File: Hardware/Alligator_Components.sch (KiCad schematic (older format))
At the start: 66 parts, among them J1 SWD_Header, J8 Eurorack_16_pin_power, U1 STM32F446RETx, U3 MCP6004, U4 PCM5100APW, U5 TL072, U7 LM1117-3.3, Y1 8MHz 20pF

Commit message: Updates to schematic; Output ADC data over I2S via interrupt with L/R awareness
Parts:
- removed C? (x2): 2.2uF, symbol Device:C_Small
- removed C? (x2): 30pF, symbol Device:C_Small
- removed C? (x6): 100nF, symbol Device:C_Small
- removed J8: Eurorack_16_pin_power, Custom_Footprints:Eurorack_16_pin_header, symbol Eurorack_Header:Eurorack_16_pin_power
- removed U1: STM32F446RETx, Package_QFP:LQFP-64_10x10mm_P0.5mm, symbol MCU_ST_STM32F4:STM32F446RETx
- removed U?: STM32H743VITx, Package_QFP:LQFP-100_14x14mm_P0.5mm, symbol MCU_ST_STM32H7:STM32H743VITx
- added C1, C10, C11, C12, C14, C15, C16, C19, C20, C21, C25, C26, C37, C42, C44, C5, C7, C8, C9: 100nF, symbol Device:C_Small
- added C2, C3: 30pF, symbol Device:C_Small
- added C4, C6: 2.2uF, symbol Device:C_Small
- added J2: Eurorack_10_pin_power, Custom_Footprints:Eurorack_10_pin_header, symbol Eurorack_Header:Eurorack_10_pin_power
- added J3: Conn_01x20_Female, symbol Connector:Conn_01x20_Female
- added U1: STM32H743ZITx, Package_QFP:LQFP-144_20x20mm_P0.5mm, symbol MCU_ST_STM32H7:STM32H743ZITx
- gave numbers to parts that had none: 1
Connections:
- net labels added: ADC123_INP11, ADC12_INP14, ADC12_INP15, ADC12_INP18, ADC12_INP19, ADC12_INP3, ADC12_INP4, ADC12_INP5, ADC12_INP7, ADC12_INP8, ADC12_INP9, ADC1_INP16, ADC1_INP17, CV_IN1, CV_IN2, CV_IN3, CV_IN4, FMC_A0, FMC_A1, FMC_A10, FMC_A11, FMC_A2, FMC_A3, FMC_A4, FMC_A5, FMC_A6, FMC_A7, FMC_A8, FMC_A9, FMC_BA0, FMC_BA1, FMC_D0, FMC_D1, FMC_D10, FMC_D11, FMC_D12, FMC_D13, FMC_D14, FMC_D15, FMC_D2, FMC_D3, FMC_D4, FMC_D5, FMC_D6, FMC_D7, FMC_D8, FMC_D9, FMC_SDCKE1, FMC_SDCLK, FMC_SD~E1, FMC_SD~WE, FMC_~BL0, FMC_~BL1, FMC_~CAS, FMC_~RAS
- net labels removed: ADC_CS, ADC_Clock, ADC_Data, CTUNE, CV_IN, Calibration, FPGA_DONE, FTUNE, HARM1_CVIN, HARM1_POT, HARM2_CVIN, HARM2_POT, HARM_COUNT_POT, PITCH_CVIN, WARP_CVIN, WARP_POT
- wire segments 260 -> 413
- no-connect marks 32 -> 56
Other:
- note removed: "Pins 19, 32, 48, 64 ground capacitors"
- moved on the sheet: C39, J1, U2

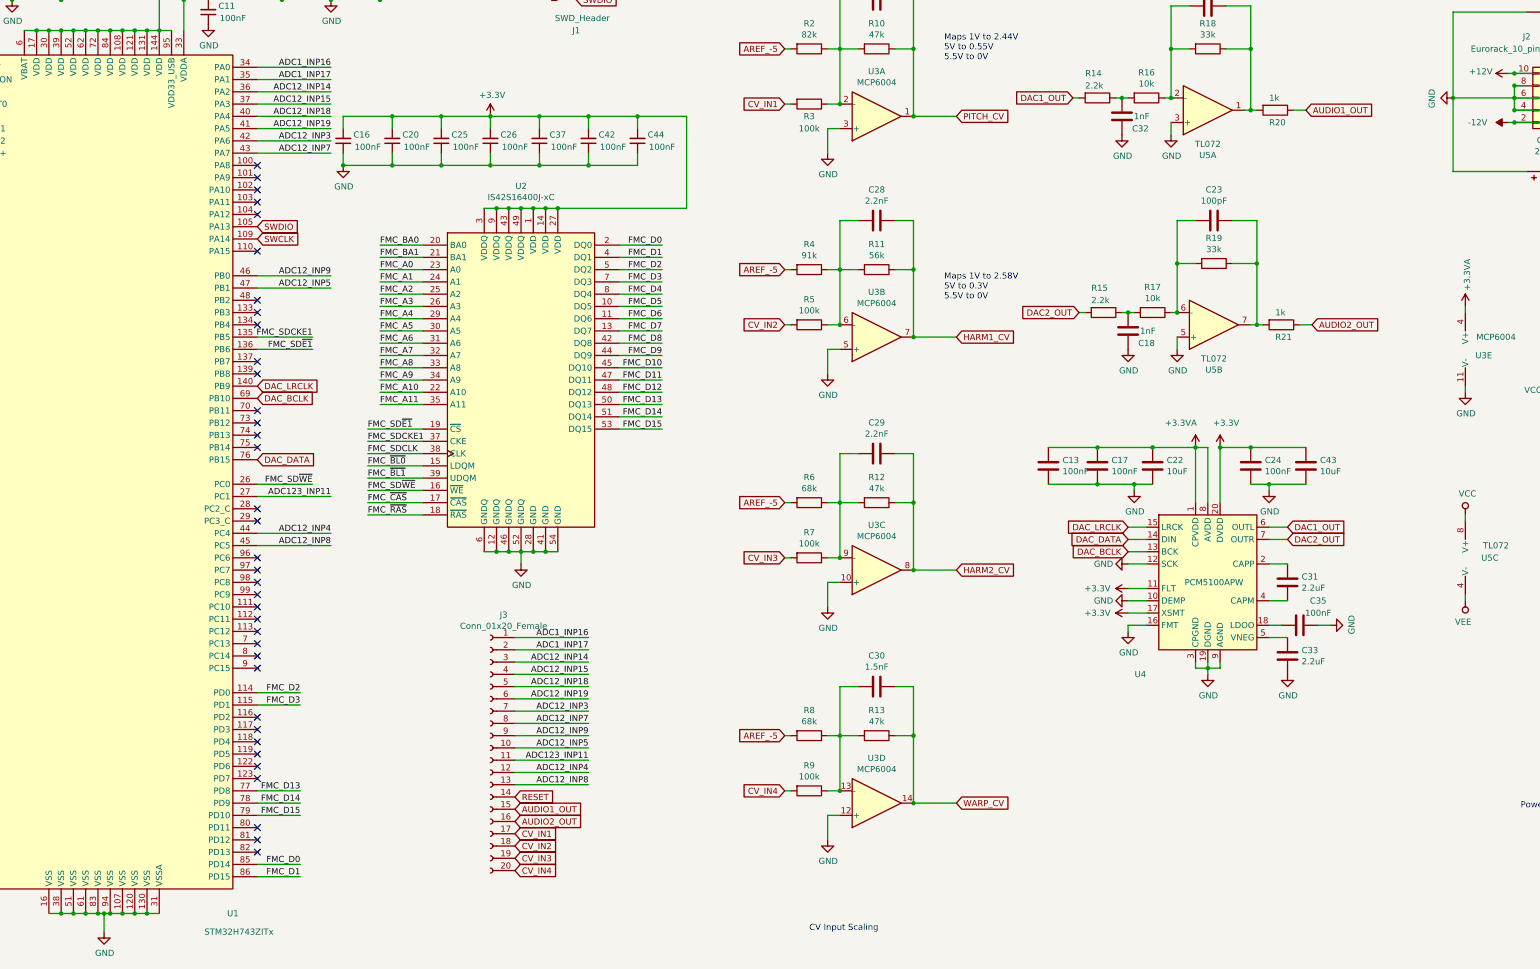
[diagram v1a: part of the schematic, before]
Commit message: Moved delay functionality to digitalDelay class; further working smoothing delay rate transitions
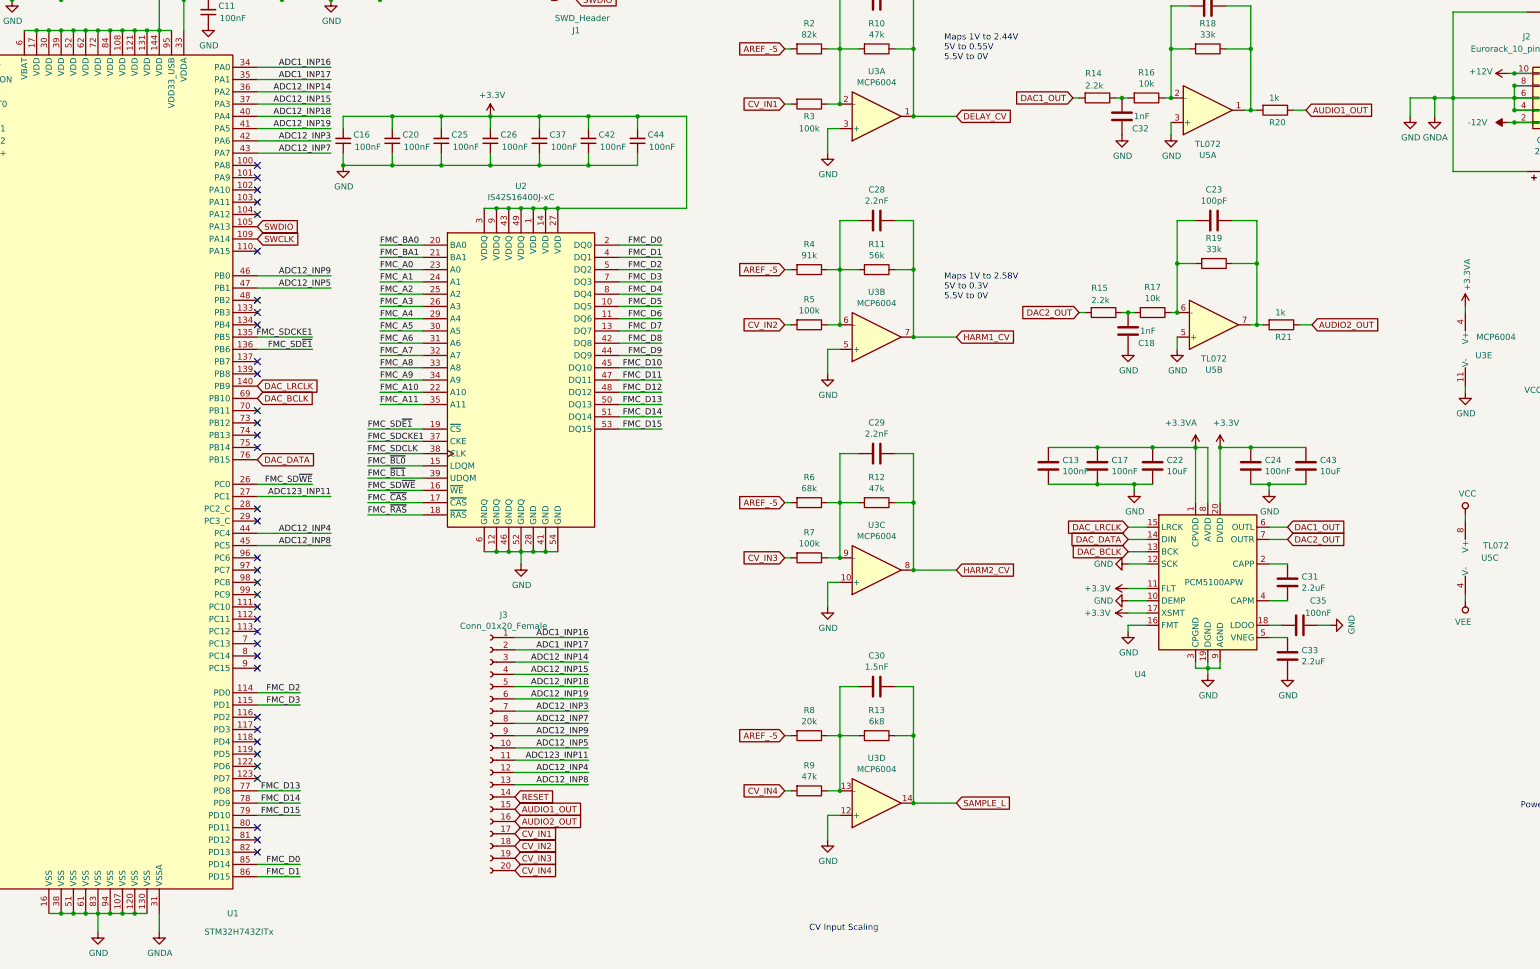
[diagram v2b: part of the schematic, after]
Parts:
- R13: value 47k -> 6k8
- R8: value 68k -> 20k
- R9: value 100k -> 47k
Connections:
- net PITCH_CV renamed DELAY_CV
- net WARP_CV renamed SAMPLE_L
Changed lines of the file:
@@
 $EndComp
 Text GLabel 9750 2350 2    50   Input ~ 0
-PITCH_CV
+DELAY_CV
 Wire Wire Line
 	9750 2350 9400 2350
@@
 $EndComp
 Text GLabel 9750 7950 2    50   Input ~ 0
-WARP_CV
+SAMPLE_L
 Wire Wire Line
 	9750 6050 9400 6050
@@
 P 9100 7400
 F 0 "R13" V 8893 7400 50  0000 C CNN
-F 1 "47k" V 8984 7400 50  0000 C CNN
+F 1 "6k8" V 8984 7400 50  0000 C CNN
 F 2 "Resistors_SMD:R_0805_HandSoldering" V 9030 7400 50  0001 C CNN
 F 3 "~" H 9100 7400 50  0001 C CNN
@@
 P 8550 7400
 F 0 "R8" V 8343 7400 50  0000 C CNN
-F 1 "68k" V 8434 7400 50  0000 C CNN
+F 1 "20k" V 8434 7400 50  0000 C CNN
 F 2 "Resistors_SMD:R_0805_HandSoldering" V 8480 7400 50  0001 C CNN
 F 3 "~" H 8550 7400 50  0001 C CNN
@@
 P 8550 7850
 F 0 "R9" V 8343 7850 50  0000 C CNN
-F 1 "100k" V 8434 7850 50  0000 C CNN
+F 1 "47k" V 8434 7850 50  0000 C CNN
 F 2 "Resistors_SMD:R_0805_HandSoldering" V 8480 7850 50  0001 C CNN
 F 3 "~" H 8550 7850 50  0001 C CNN
@@
 L power:GND #PWR066
 U 1 1 5C9E963D
-P 13800 2200
-F 0 "#PWR066" H 13800 1950 50  0001 C CNN
-F 1 "GND" H 13805 2027 50  0000 C CNN
-F 2 "" H 13800 2200 50  0001 C CNN
-F 3 "" H 13800 2200 50  0001 C CNN
-	1    13800 2200
-	0    1    1    0
+P 13450 2350
+F 0 "#PWR066" H 13450 2100 50  0001 C CNN
+F 1 "GND" H 13455 2177 50  0000 C CNN
+F 2 "" H 13450 2350 50  0001 C CNN
+F 3 "" H 13450 2350 50  0001 C CNN
+	1    13450 2350
+	1    0    0    -1
 $EndComp
 $Comp
@@
 L power:GND #PWR0102
 U 1 1 5F0205DB
-P 2800 9000
-F 0 "#PWR0102" H 2800 8750 50  0001 C CNN
-F 1 "GND" H 2805 8827 50  0000 C CNN
-F 2 "" H 2800 9000 50  0001 C CNN
-F 3 "" H 2800 9000 50  0001 C CNN
-	1    2800 9000
+P 2750 9000
+F 0 "#PWR0102" H 2750 8750 50  0001 C CNN
+F 1 "GND" H 2755 8827 50  0000 C CNN
+F 2 "" H 2750 9000 50  0001 C CNN
+F 3 "" H 2750 9000 50  0001 C CNN
+	1    2750 9000
 	1    0    0    -1
 $EndComp
@@
 	1    0    0    -1
 $EndComp
-Wire Wire Line
-	2800 9000 2800 8850
 Wire Wire Line
 	4400 8450 4050 8450
@@
 Connection ~ 2750 8850
 Wire Wire Line
-	2750 8850 2800 8850
-Wire Wire Line
 	2550 8850 2650 8850
 Connection ~ 2850 8850
@@
 Wire Wire Line
 	3050 8850 3150 8850
-Connection ~ 3150 8850
-Wire Wire Line
-	3150 8850 3250 8850
-Connection ~ 2800 8850
-Wire Wire Line
-	2800 8850 2850 8850
 Connection ~ 3250 1650
 Wire Wire Line
@@
 	-1   0    0    -1
 $EndComp
+$Comp
+L power:GNDA #PWR?
+U 1 1 5F0C7244
+P 13650 2350
+F 0 "#PWR?" H 13650 2100 50  0001 C CNN
+F 1 "GNDA" H 13655 2177 50  0000 C CNN
+F 2 "" H 13650 2350 50  0001 C CNN
+F 3 "" H 13650 2350 50  0001 C CNN
+	1    13650 2350
+	1    0    0    -1
+$EndComp
+Wire Wire Line
+	13450 2350 13450 2200
+Wire Wire Line
+	13450 2200 13650 2200
+Wire Wire Line
+	13650 2350 13650 2200
+Connection ~ 13650 2200
+Wire Wire Line
+	13650 2200 13800 2200
+$Comp
+L power:GNDA #PWR?
+U 1 1 5F182A43
+P 3250 9000
+F 0 "#PWR?" H 3250 8750 50  0001 C CNN
+F 1 "GNDA" H 3255 8827 50  0000 C CNN
+F 2 "" H 3250 9000 50  0001 C CNN
+F 3 "" H 3250 9000 50  0001 C CNN
+	1    3250 9000
+	1    0    0    -1
+$EndComp
+Wire Wire Line
+	3250 8850 3250 9000
+Wire Wire Line
+	2750 8850 2850 8850
+Wire Wire Line
+	2750 8850 2750 9000
 $EndSCHEMATC

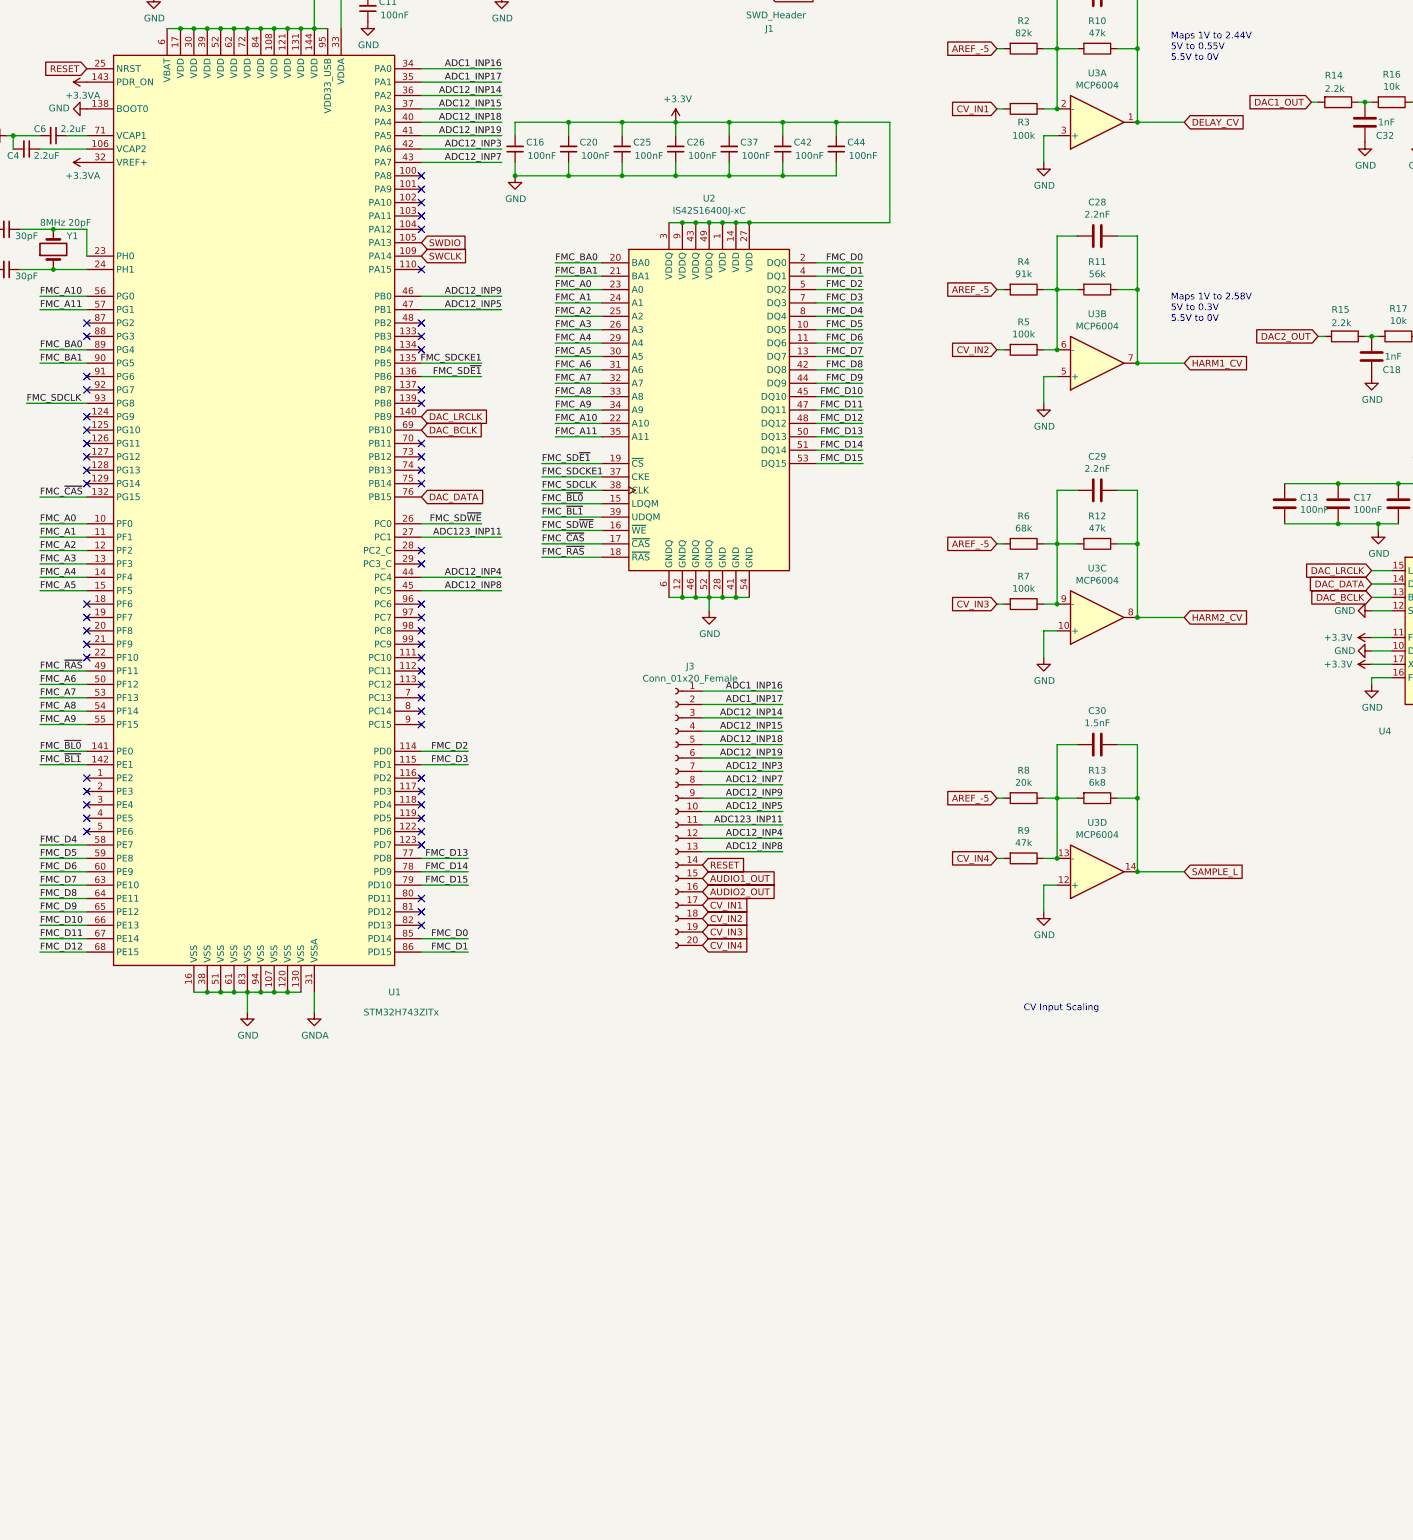
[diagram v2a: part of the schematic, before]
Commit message: Added initialisation and test code for DAC output; Schematic changes for first attempt at Wet/Dry mixer
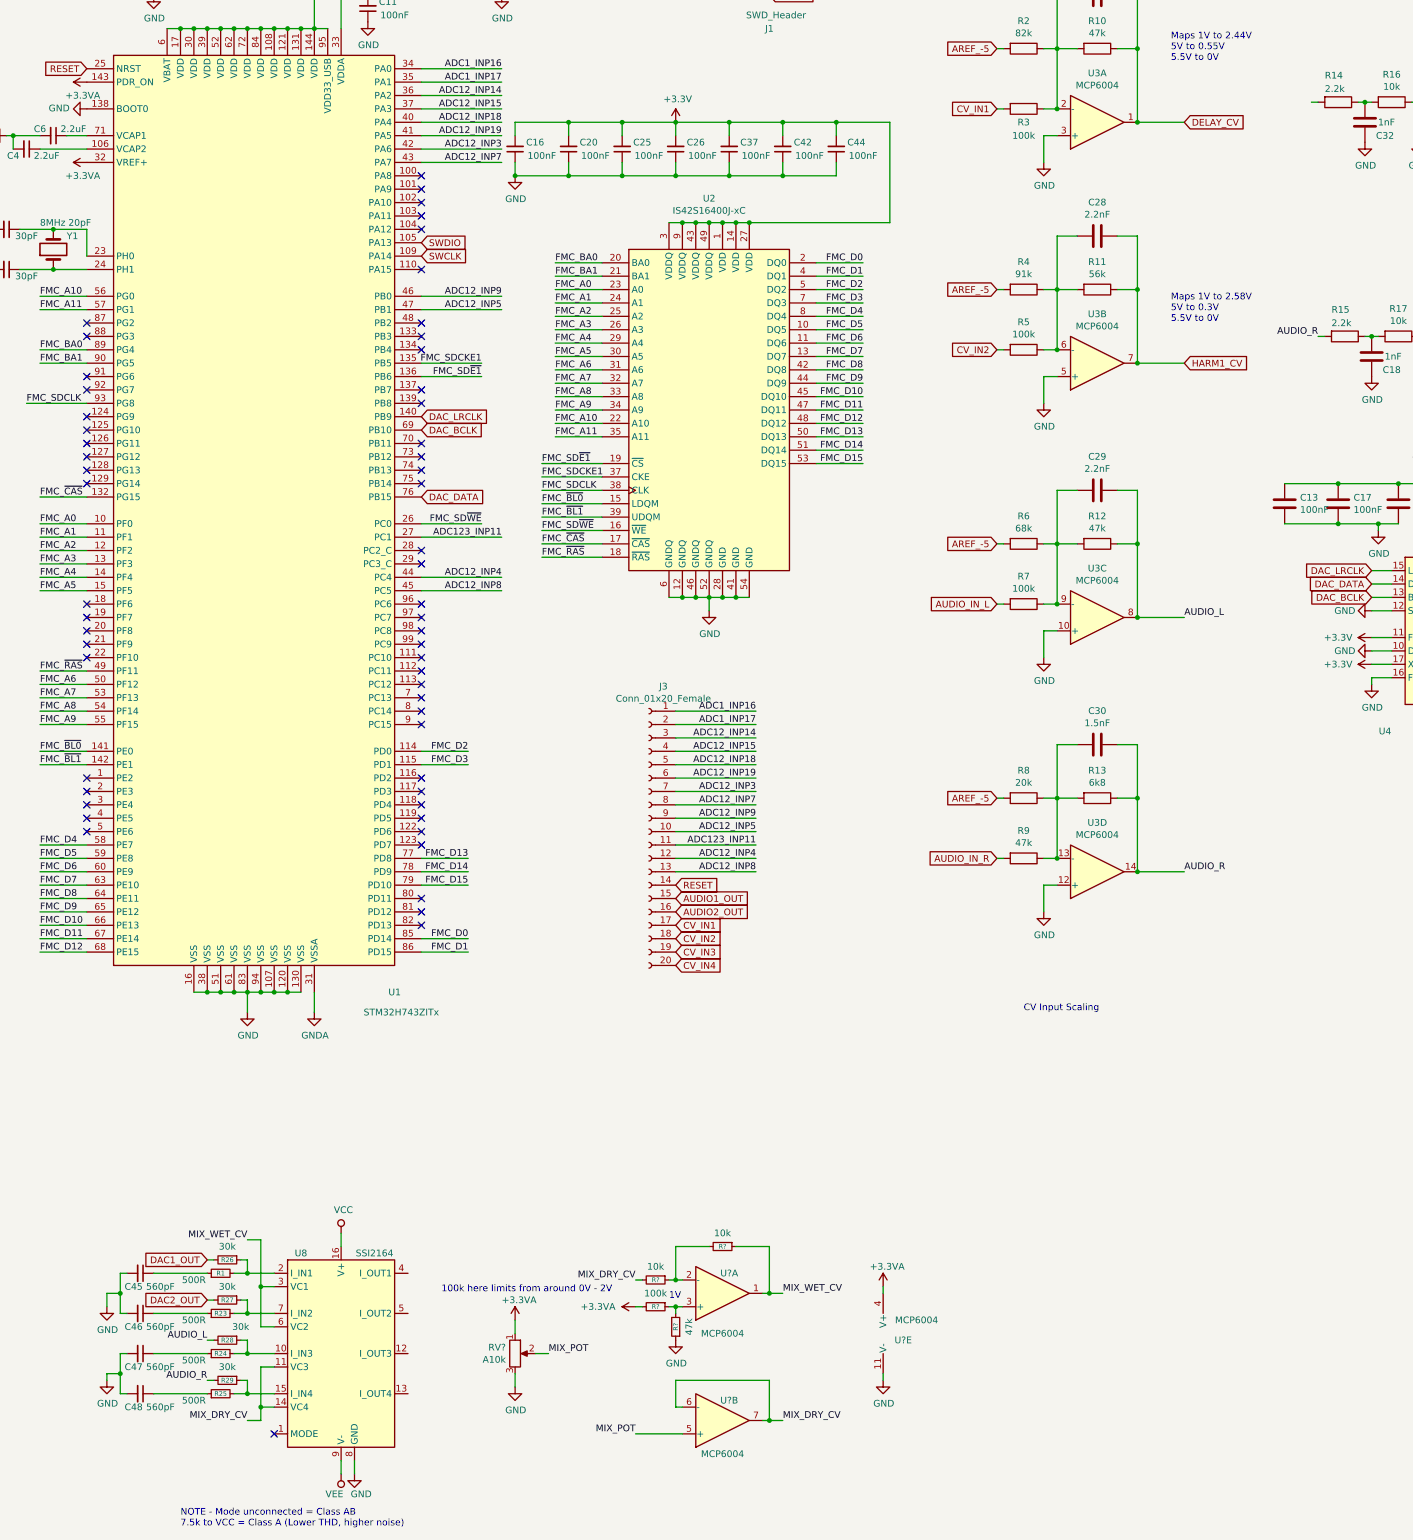
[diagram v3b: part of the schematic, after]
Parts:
- added C45, C46, C47, C48: 560pF, symbol Device:C_Small
- added R1, R23, R24, R25: 500R, symbol Device:R_Small
- added R26, R27, R28, R29: 30k, symbol Device:R_Small
- added R? (x2): 10k, symbol Device:R_Small
- added R?: 100k, symbol Device:R_Small
- added R?: 47k, symbol Device:R_Small
- added RV?: A10k, symbol Device:R_POT
- added U8: SSI2164, Package_SO:SOIC-16_3.9x9.9mm_P1.27mm, symbol Audio:SSI2164
- added U? (x3): MCP6004, SMD_Packages:SOIC-14_N, symbol Amplifier_Operational:MCP6004
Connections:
- net +3.3VA: now also R?.2, RV?.1, U?.4 (V+)
- net CV_IN3: no longer R7.2
- net CV_IN4: no longer R9.2
- net DAC1_OUT: now also R26.2; no longer R14.2
- net DAC2_OUT: now also R27.2; no longer R15.2
- net GND: now also C45.2, C46.2, C47.2, C48.2, R?.1, RV?.3, U8.8 (GND), U?.11 (V-)
- net VCC: now also U8.16 (V+)
- net VEE: now also U8.9 (V-)
- net HARM2_CV renamed AUDIO_L
- net AUDIO_L: now also R28.2
- net SAMPLE_L renamed AUDIO_R
- net AUDIO_R: now also R15.2, R29.2
- new net: R24.2, R28.1, U8.10 (I_IN3)
- new net: R25.2, R29.1, U8.15 (I_IN4)
- new net: R1.2, R26.1, U8.2 (I_IN1)
- new net: R23.2, R27.1, U8.7 (I_IN2)
- new net: C45.1, R1.1
- new net: R?.1, R?.2, U?.2 (-)
- new net: C46.1, R23.1
- new net: C47.1, R24.1
- new net: C48.1, R25.1
- new net: R?.1, R?.2, U?.3 (+)
- new net AUDIO_IN_L: R7.2
- new net AUDIO_IN_R: R9.2
- new net MIX_DRY_CV: R?.2, U8.11 (VC3), U8.14 (VC4), U?.6 (-), U?.7
- new net MIX_POT: RV?.2, U?.5 (+)
- new net MIX_WET_CV: R?.1, U8.3 (VC1), U8.6 (VC2), U?.1
- no-connect marks 56 -> 57
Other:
- note added: "100k here limits from around 0V - 2V"
- note added: "1V"
- note added: "NOTE - Mode unconnected = Class AB\n7.5k to VCC = Class A (Lower THD, higher noise)"
- moved on the sheet: J3
